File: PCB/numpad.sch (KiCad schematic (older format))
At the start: 81 parts, among them J1 AVR-ISP-6, SW1 SW_Push

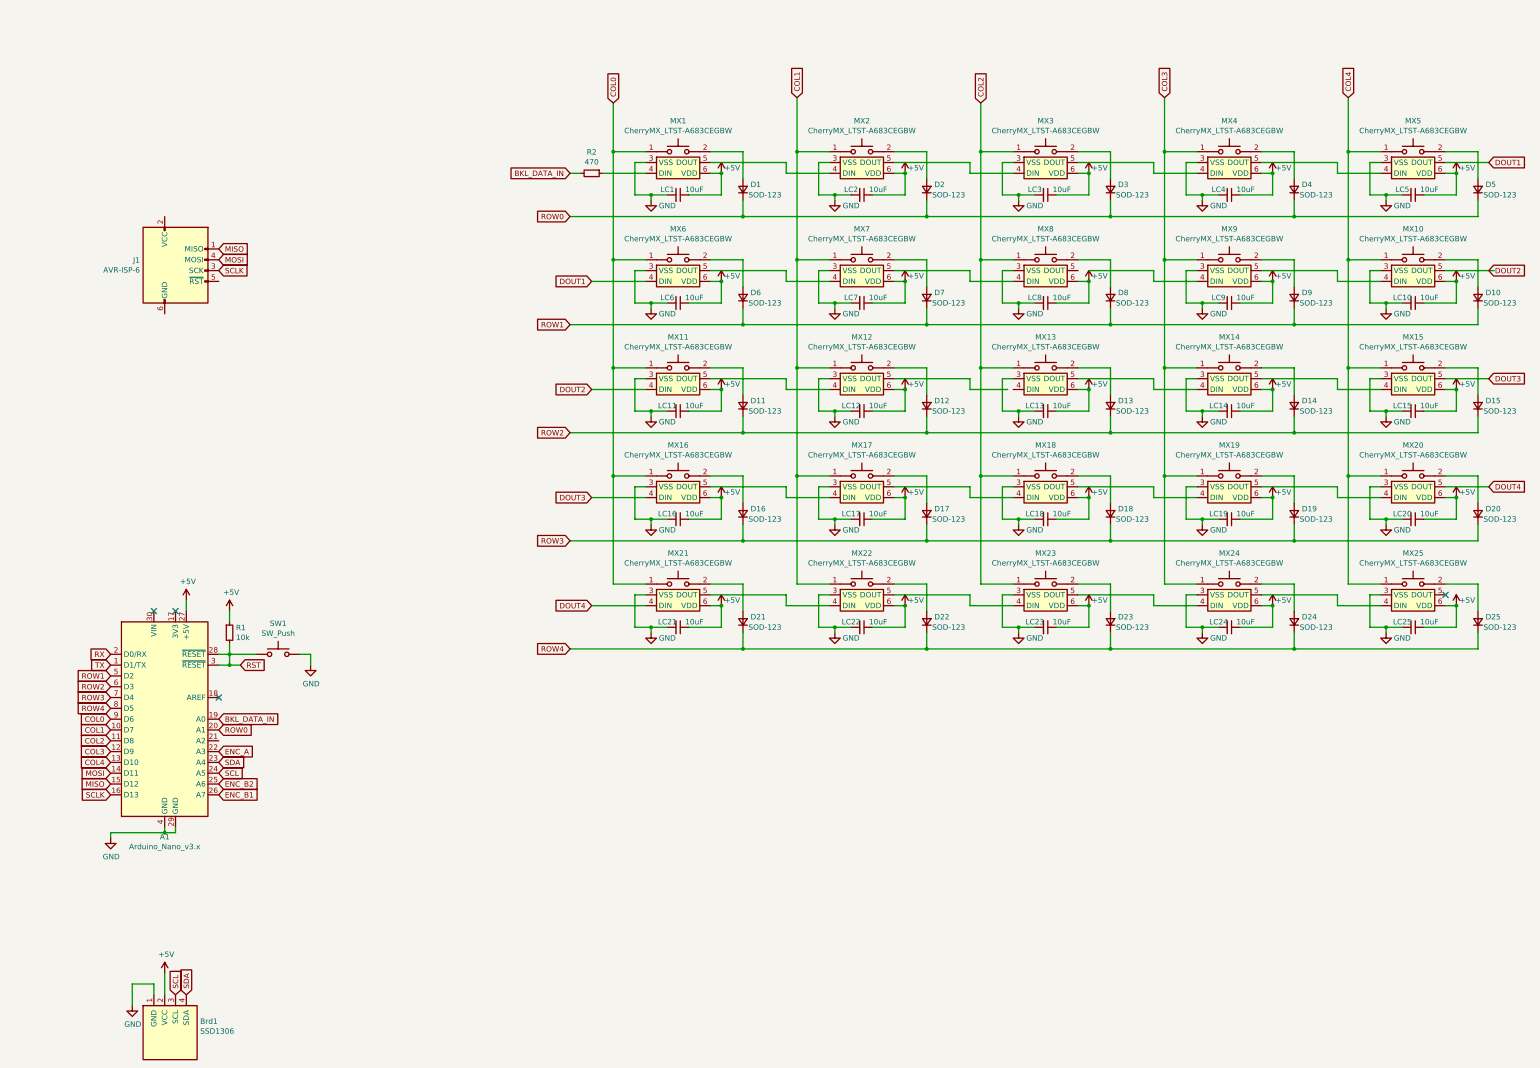
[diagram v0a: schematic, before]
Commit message: Switched to Pro Micro
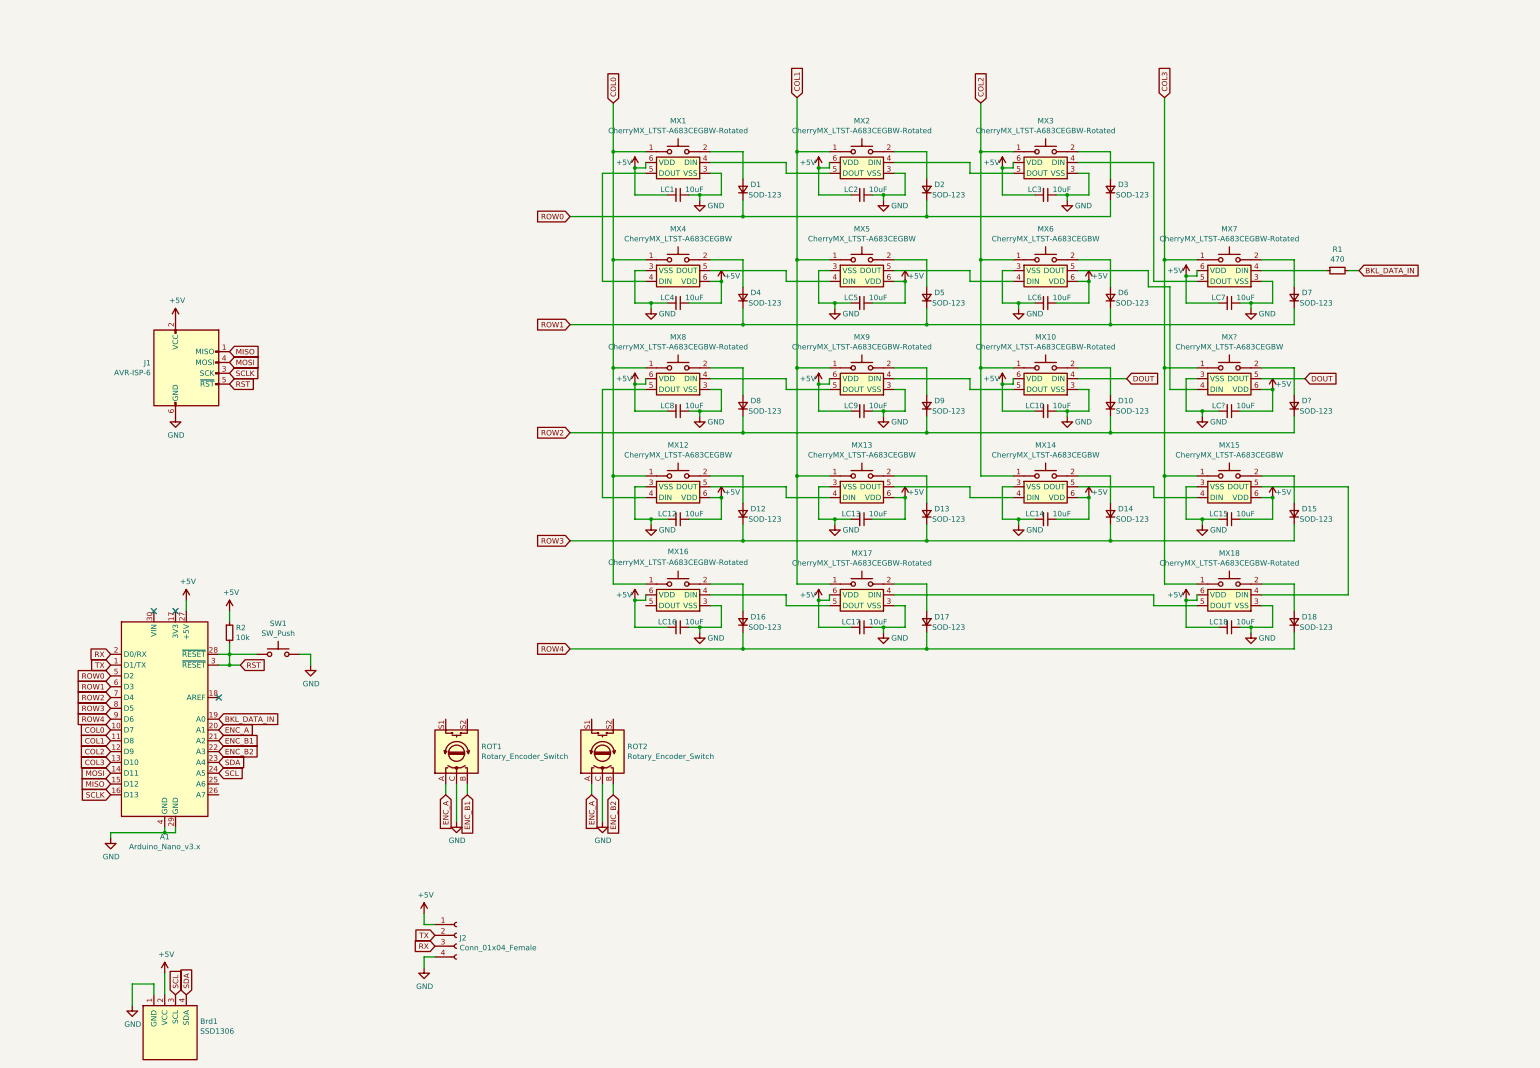
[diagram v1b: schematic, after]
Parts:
- removed D11, D12, D13, D14, D15, D20, D21, D22, D23, D24, D25, D4, D5: SOD-123, Diode_SMD:D_SOD-123, symbol Device:D_Small
- removed LC11, LC12, LC13, LC14, LC15, LC20, LC21, LC22, LC23, LC24, LC25, LC4, LC5: 10uF, Capacitor_SMD:C_0805_2012Metric, symbol Device:C_Small
- removed MX1, MX10, MX11, MX12, MX13, MX14, MX15, MX2, MX20, MX21, MX22, MX23, MX24, MX25, MX3, MX4, MX5, MX9: CherryMX_LTST-A683CEGBW, CherryMX_PCB_KailhSocket_LTST-A683CEGBW:CherryMX_1.00u_PCB_KailhSocket_LTST-A683CEGBW, symbol CherryMX:CherryMX_LTST-A683CEGBW
- added D16, D17, D18, D7, D8, D?: SOD-123, Diode_SMD:D_SOD-123, symbol Device:D_Small
- added J2: Conn_01x04_Female, Connector_PinHeader_2.54mm:PinHeader_1x04_P2.54mm_Vertical, symbol Connector:Conn_01x04_Female
- added LC16, LC17, LC18, LC7, LC8, LC?: 10uF, Capacitor_SMD:C_0805_2012Metric, symbol Device:C_Small
- added MX1, MX10, MX17, MX18, MX2, MX3, MX7, MX8, MX9: CherryMX_LTST-A683CEGBW-Rotated, CherryMX_PCB_KailhSocket_LTST-A683CEGBW-Rotated:CherryMX_1.00u_PCB_KailhSocket_LTST-A683CEGBW-Rotated, symbol CherryMX:CherryMX_LTST-A683CEGBW-Rotated
- added MX16: CherryMX_LTST-A683CEGBW-Rotated, CherryMX_PCB_KailhSocket_StabWireBottom_LTST-A683CEGBW-Rotated:CherryMX_2.00u_PCB_KailhSocket_StabWireBottom_LTST-A683C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, symbol CherryMX:CherryMX_LTST-A683CEGBW-Rotated
- added MX?: CherryMX_LTST-A683CEGBW, CherryMX_KailhSocket_StabWireBottom_LTST-A683CEGBW:CherryMX_2.00u_KailhSocket_StabWireBottom_LTST-A683CEGBW, symbol CherryMX:CherryMX_LTST-A683CEGBW
- added ROT1, ROT2: Rotary_Encoder_Switch, Rotary_Encoder:RotaryEncoder_Alps_EC11E-Switch_Vertical_H20mm, symbol Device:Rotary_Encoder_Switch
- J1: footprint Connector_PinHeader_2.54mm:PinHeader_1x04_P2.54mm_Vertical -> Connector_PinHeader_2.54mm:PinHeader_2x03_P2.54mm_Vertical
- MX15: renamed from MX19; footprint CherryMX_PCB_KailhSocket_LTST-A683CEGBW:CherryMX_1.00u_PCB_KailhSocket_LTST-A683CEGBW -> CherryMX_KailhSocket_StabWireBottom_LTST-A683CEGBW:CherryMX_2.00u_KailhSocket_StabWireBottom_LTST-A683CEGBW
- renumbered D16 to D12, D17 to D13, D18 to D14, D19 to D15, D6 to D4, D7 to D5, D8 to D6, LC16 to LC12, LC17 to LC13, LC18 to LC14, LC19 to LC15, LC6 to LC4, LC7 to LC5, LC8 to LC6, MX16 to MX12, MX17 to MX13, MX18 to MX14, MX6 to MX4, MX7 to MX5, MX8 to MX6, R2 to R1, R1 to R2
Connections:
- net COL4 is gone; now on net COL3: A1.13 (D10)
- net +5V: now also J1.2 (VCC), LC1.2, LC10.2, LC2.2, LC3.2, LC9.2, J2.1 (Pin_1), LC16.2, LC17.2, LC18.2, LC7.2, LC8.2, LC?.1, MX1.6 (VDD), MX10.6 (VDD), MX16.6 (VDD), MX17.6 (VDD), MX18.6 (VDD), MX2.6 (VDD), MX3.6 (VDD), MX7.6 (VDD), MX8.6 (VDD), MX9.6 (VDD), MX?.6 (VDD); no longer LC1.1, LC10.1, LC2.1, LC3.1, LC9.1
- net COL0: now also A1.10 (D7), MX1.1, MX16.1, MX8.1; no longer A1.9 (D6)
- net COL1: now also A1.11 (D8), MX17.1, MX2.1, MX9.1; no longer A1.10 (D7)
- net COL2: now also A1.12 (D9), MX10.1, MX3.1; no longer A1.11 (D8)
- net COL3: now also MX18.1, MX7.1, MX?.1; no longer A1.12 (D9)
- net ENC_A: now also A1.20 (A1), ROT1.A, ROT2.A; no longer A1.22 (A3)
- net ENC_B1: now also A1.21 (A2), ROT1.B; no longer A1.26 (A7)
- net ENC_B2: now also A1.22 (A3), ROT2.B; no longer A1.25 (A6)
- net GND: now also J1.6 (GND), LC1.1, LC10.1, LC2.1, LC3.1, LC9.1, J2.4 (Pin_4), LC16.1, LC17.1, LC18.1, LC7.1, LC8.1, LC?.2, MX1.3 (VSS), MX10.3 (VSS), MX16.3 (VSS), MX17.3 (VSS), MX18.3 (VSS), MX2.3 (VSS), MX3.3 (VSS), MX7.3 (VSS), MX8.3 (VSS), MX9.3 (VSS), MX?.3 (VSS), ROT1.C, ROT2.C; no longer LC1.2, LC10.2, LC2.2, LC3.2, LC9.2
- net ROW0: now also A1.5 (D2); no longer A1.20 (A1)
- net ROW1: now also A1.6 (D3), D7.1 (K); no longer A1.5 (D2), D10.1 (K), D9.1 (K)
- net ROW2: now also A1.7 (D4), D10.1 (K), D9.1 (K), D8.1 (K), D?.1 (K); no longer A1.6 (D3)
- net ROW3: now also A1.8 (D5); no longer A1.7 (D4)
- net ROW4: now also A1.9 (D6), D16.1 (K), D17.1 (K), D18.1 (K); no longer A1.8 (D5)
- net RST: now also J1.5 (~RST)
- net RX: now also J2.3 (Pin_3)
- net TX: now also J2.2 (Pin_2)
- net at D1.2 (A): now also MX1.2
- net at R1.1: now also MX7.4 (DIN)
- net at D2.2 (A): now also MX2.2
- net at D3.2 (A): now also MX3.2
- net at MX6.5 (DOUT): now also MX?.4 (DIN)
- net at D9.2 (A): now also MX9.2
- net at D10.2 (A): now also MX10.2
- net at MX15.5 (DOUT): now also MX18.4 (DIN)
- net DOUT1: no longer names the net of MX4.4 (DIN)
- net DOUT1: now also MX1.5 (DOUT)
- net DOUT3: no longer names the net of MX12.4 (DIN)
- net DOUT3: now also MX8.5 (DOUT)
- new net: MX1.4 (DIN), MX2.5 (DOUT)
- new net: MX2.4 (DIN), MX3.5 (DOUT)
- new net: MX3.4 (DIN), MX7.5 (DOUT)
- new net: D7.2 (A), MX7.2
- new net: D8.2 (A), MX8.2
- new net: MX8.4 (DIN), MX9.5 (DOUT)
- new net: MX10.5 (DOUT), MX9.4 (DIN)
- new net: D16.2 (A), MX16.2
- new net: MX16.4 (DIN), MX17.5 (DOUT)
- new net: D17.2 (A), MX17.2
- new net: MX17.4 (DIN), MX18.5 (DOUT)
- new net: D18.2 (A), MX18.2
- new net: D?.2 (A), MX?.2
- new net DOUT: MX10.4 (DIN), MX?.5 (DOUT)
- no-connect marks 4 -> 3
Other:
- moved on the sheet: J1, R1

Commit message: Refined traces and schematic for review
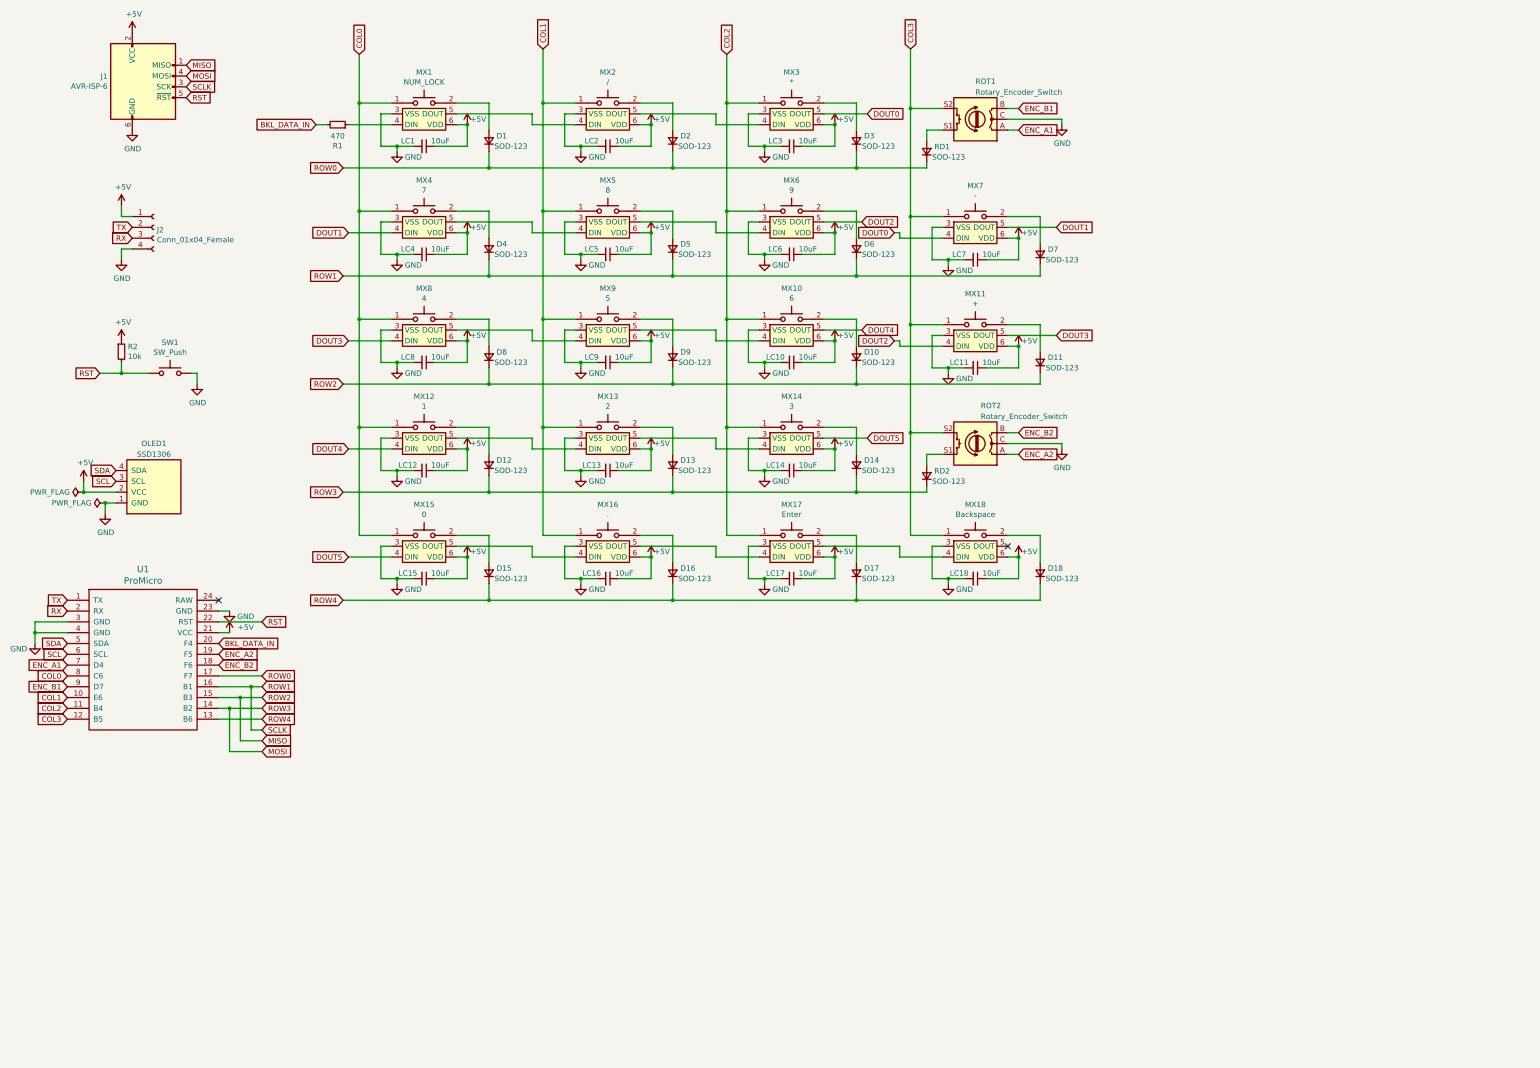
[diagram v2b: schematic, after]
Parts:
- removed A1: Arduino_Nano_v3.x, Module:Arduino_Nano, symbol MCU_Module:Arduino_Nano_v3.x
- removed D?: SOD-123, Diode_SMD:D_SOD-123, symbol Device:D_Small
- removed LC?: 10uF, Capacitor_SMD:C_0805_2012Metric, symbol Device:C_Small
- removed MX1, MX10, MX17, MX18, MX2, MX3, MX7, MX8, MX9: CherryMX_LTST-A683CEGBW-Rotated, CherryMX_PCB_KailhSocket_LTST-A683CEGBW-Rotated:CherryMX_1.00u_PCB_KailhSocket_LTST-A683CEGBW-Rotated, symbol CherryMX:CherryMX_LTST-A683CEGBW-Rotated
- removed MX16: CherryMX_LTST-A683CEGBW-Rotated, CherryMX_PCB_KailhSocket_StabWireBottom_LTST-A683CEGBW-Rotated:CherryMX_2.00u_PCB_KailhSocket_StabWireBottom_LTST-A683C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, symbol CherryMX:CherryMX_LTST-A683CEGBW-Rotated
- removed MX?: CherryMX_LTST-A683CEGBW, CherryMX_KailhSocket_StabWireBottom_LTST-A683CEGBW:CherryMX_2.00u_KailhSocket_StabWireBottom_LTST-A683CEGBW, symbol CherryMX:CherryMX_LTST-A683CEGBW
- added D11, RD1, RD2: SOD-123, Diode_SMD:D_SOD-123, symbol Device:D_Small
- added LC11: 10uF, Capacitor_SMD:C_0805_2012Metric, symbol Device:C_Small
- added MX1: NUM_LOCK, CherryMX_PCB_KailhSocket_LTST-A683CEGBW:CherryMX_1.00u_PCB_KailhSocket_LTST-A683CEGBW, symbol CherryMX:CherryMX_LTST-A683CEGBW
- added MX10: 6, CherryMX_PCB_KailhSocket_LTST-A683CEGBW:CherryMX_1.00u_PCB_KailhSocket_LTST-A683CEGBW, symbol CherryMX:CherryMX_LTST-A683CEGBW
- added MX11: +, CherryMX_KailhSocket_StabWireBottom_LTST-A683CEGBW:CherryMX_2.00u_KailhSocket_StabWireBottom_LTST-A683CEGBW, symbol CherryMX:CherryMX_LTST-A683CEGBW
- added MX16: ., CherryMX_PCB_KailhSocket_LTST-A683CEGBW:CherryMX_1.00u_PCB_KailhSocket_LTST-A683CEGBW, symbol CherryMX:CherryMX_LTST-A683CEGBW
- added MX17: Enter, CherryMX_KailhSocket_StabWireBottom_LTST-A683CEGBW:CherryMX_2.00u_KailhSocket_StabWireBottom_LTST-A683CEGBW, symbol CherryMX:CherryMX_LTST-A683CEGBW
- added MX18: Backspace, CherryMX_PCB_KailhSocket_LTST-A683CEGBW:CherryMX_1.00u_PCB_KailhSocket_LTST-A683CEGBW, symbol CherryMX:CherryMX_LTST-A683CEGBW
- added MX2: /, CherryMX_PCB_KailhSocket_LTST-A683CEGBW:CherryMX_1.00u_PCB_KailhSocket_LTST-A683CEGBW, symbol CherryMX:CherryMX_LTST-A683CEGBW
- added MX3: *, CherryMX_PCB_KailhSocket_LTST-A683CEGBW:CherryMX_1.00u_PCB_KailhSocket_LTST-A683CEGBW, symbol CherryMX:CherryMX_LTST-A683CEGBW
- added MX7: -, CherryMX_PCB_KailhSocket_LTST-A683CEGBW:CherryMX_1.00u_PCB_KailhSocket_LTST-A683CEGBW, symbol CherryMX:CherryMX_LTST-A683CEGBW
- added MX8: 4, CherryMX_PCB_KailhSocket_LTST-A683CEGBW:CherryMX_1.00u_PCB_KailhSocket_LTST-A683CEGBW, symbol CherryMX:CherryMX_LTST-A683CEGBW
- added MX9: 5, CherryMX_PCB_KailhSocket_LTST-A683CEGBW:CherryMX_1.00u_PCB_KailhSocket_LTST-A683CEGBW, symbol CherryMX:CherryMX_LTST-A683CEGBW
- added U1: ProMicro, promicro:ProMicro, symbol promicro:ProMicro
- D1, D10, D12, D13, D14, D15, D16, D17, D18, D2, D3, D4, D5, D6, D7, D8, D9: LCSC Part (none) -> C81598
- J1, J2, ROT1, ROT2: JLCPCB BOM (none) -> 0
- LC1, LC10, LC12, LC13, LC14, LC15, LC16, LC17, LC18, LC2, LC3, LC4, LC5, LC6, LC7, LC8, LC9: LCSC Part (none) -> C15850
- MX12: value CherryMX_LTST-A683CEGBW -> 1; JLCPCB BOM (none) -> 0
- MX13: value CherryMX_LTST-A683CEGBW -> 2; JLCPCB BOM (none) -> 0
- MX14: value CherryMX_LTST-A683CEGBW -> 3; JLCPCB BOM (none) -> 0
- MX15: value CherryMX_LTST-A683CEGBW -> 0; JLCPCB BOM (none) -> 0
- MX4: value CherryMX_LTST-A683CEGBW -> 7; JLCPCB BOM (none) -> 0
- MX5: value CherryMX_LTST-A683CEGBW -> 8; JLCPCB BOM (none) -> 0
- MX6: value CherryMX_LTST-A683CEGBW -> 9; JLCPCB BOM (none) -> 0
- OLED1: renamed from Brd1; JLCPCB BOM (none) -> 0
- R1: LCSC Part (none) -> C17710
- R2: LCSC Part (none) -> C17414
- SW1: LCSC Part (none) -> C318884
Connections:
- net ROW2 is gone; now on net MISO: D10.1 (K), D8.1 (K), D9.1 (K)
- net SCLK is gone; now on net ROW1: J1.3 (SCK)
- net +5V: now also LC1.1, LC10.1, LC16.1, LC17.1, LC18.1, LC2.1, LC3.1, LC7.1, LC8.1, LC9.1, LC11.1, MX1.6 (VDD), MX10.6 (VDD), MX11.6 (VDD), MX16.6 (VDD), MX17.6 (VDD), MX18.6 (VDD), MX2.6 (VDD), MX3.6 (VDD), MX7.6 (VDD), MX8.6 (VDD), MX9.6 (VDD), U1.21 (VCC); no longer LC1.2, LC10.2, LC16.2, LC17.2, LC18.2, LC2.2, LC3.2, LC7.2, LC8.2, LC9.2
- net BKL_DATA_IN: now also U1.20 (F4)
- net COL0: now also MX15.1, MX1.1, MX8.1, U1.8 (C6)
- net COL1: now also MX16.1, MX2.1, MX9.1, U1.10 (E6)
- net COL2: now also MX10.1, MX17.1, MX3.1, U1.11 (B4)
- net COL3: now also ROT1.S2, ROT2.S2, MX11.1, MX18.1, MX7.1, U1.12 (B5); no longer MX15.1
- net ENC_B1: now also U1.9 (D7)
- net ENC_B2: now also U1.18 (F6)
- net GND: now also LC1.2, LC10.2, LC16.2, LC17.2, LC18.2, LC2.2, LC3.2, LC7.2, LC8.2, LC9.2, LC11.2, MX1.3 (VSS), MX10.3 (VSS), MX11.3 (VSS), MX16.3 (VSS), MX17.3 (VSS), MX18.3 (VSS), MX2.3 (VSS), MX3.3 (VSS), MX7.3 (VSS), MX8.3 (VSS), MX9.3 (VSS), U1.23 (GND), U1.3 (GND), U1.4 (GND); no longer LC1.1, LC10.1, LC16.1, LC17.1, LC18.1, LC2.1, LC3.1, LC7.1, LC8.1, LC9.1
- net MISO: now also D11.1 (K), U1.15 (B3)
- net MOSI: now also D12.1 (K), D13.1 (K), D14.1 (K), RD2.1 (K), U1.14 (B2)
- net ROW0: now also RD1.1 (K), U1.17 (F7)
- net ROW1: now also U1.16 (B1)
- net ROW4: now also D15.1 (K), U1.13 (B6)
- net RST: now also U1.22 (RST)
- net RX: now also U1.2 (RX)
- net SCL: now also U1.6 (SCL)
- net SDA: now also U1.5 (SDA)
- net TX: now also U1.1 (TX)
- net at D1.2 (A): now also MX1.2
- net DOUT1: now reaches MX4.4 (DIN)
- net DOUT1: now also MX7.5 (DOUT)
- net DOUT2: now reaches MX6.5 (DOUT)
- net DOUT2: now also MX11.4 (DIN)
- net DOUT4: now reaches MX12.4 (DIN)
- net DOUT4: now also MX10.5 (DOUT)
- net DOUT5: now reaches MX14.5 (DOUT), MX15.4 (DIN)
- net at MX15.5 (DOUT): now also MX16.4 (DIN)
- net at R1.1: now also MX1.4 (DIN)
- net at ROT1.S1: now also RD1.2 (A)
- net at ROT2.S1: now also RD2.2 (A)
- net at D2.2 (A): now also MX2.2
- net at D3.2 (A): now also MX3.2
- net at D7.2 (A): now also MX7.2
- net at D8.2 (A): now also MX8.2
- net at D9.2 (A): now also MX9.2
- net at D10.2 (A): now also MX10.2
- net at D16.2 (A): now also MX16.2
- net at D17.2 (A): now also MX17.2
- net at D18.2 (A): now also MX18.2
- net ENC_A renamed ENC_A1
- net ENC_A1: now also U1.7 (D4); no longer ROT2.A
- removed net ROW3: D12.1 (K), D13.1 (K), D14.1 (K), D15.1 (K)
- new net: MX1.5 (DOUT), MX2.4 (DIN)
- new net: MX2.5 (DOUT), MX3.4 (DIN)
- new net: MX8.5 (DOUT), MX9.4 (DIN)
- new net: MX10.4 (DIN), MX9.5 (DOUT)
- new net: D11.2 (A), MX11.2
- new net: MX16.5 (DOUT), MX17.4 (DIN)
- new net: MX17.5 (DOUT), MX18.4 (DIN)
- new net DOUT0: MX3.5 (DOUT), MX7.4 (DIN)
- new net DOUT3: MX11.5 (DOUT), MX8.4 (DIN)
- new net ENC_A2: ROT2.A, U1.19 (F5)
- no-connect marks 3 -> 2
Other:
- moved on the sheet: D4, D5, D6, J1, J2, LC4, LC5, LC6, MX4, MX5, MX6, OLED1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
